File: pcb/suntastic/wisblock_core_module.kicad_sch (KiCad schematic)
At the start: 0 parts

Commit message: Add load switch and RAK connector
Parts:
- added J4: FBB04004-F40S1003K6M, FBB04004F40S1003K6M, symbol FBB04004-F40S1003K6M:FBB04004-F40S1003K6M
- added JP11: SolderJumper_2_Open, Jumper:SolderJumper-2_P1.3mm_Open_RoundedPad1.0x1.5mm, symbol Jumper:SolderJumper_2_Open
- added R2: 5.6M, symbol Device:R
- added R3: 9.3M, symbol Device:R
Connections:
- new net: JP11.2 (B), R2.1
- new net GND: J4.3, J4.39, J4.4, J4.40, J4.MP1, J4.MP2, J4.MP3, J4.MP4, R3.2
- new net V_boost_uvlo: JP11.1 (A)
- new net Vsupercap: R2.2, R3.1
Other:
- note added: "Voltage divider to measure the accumulator"

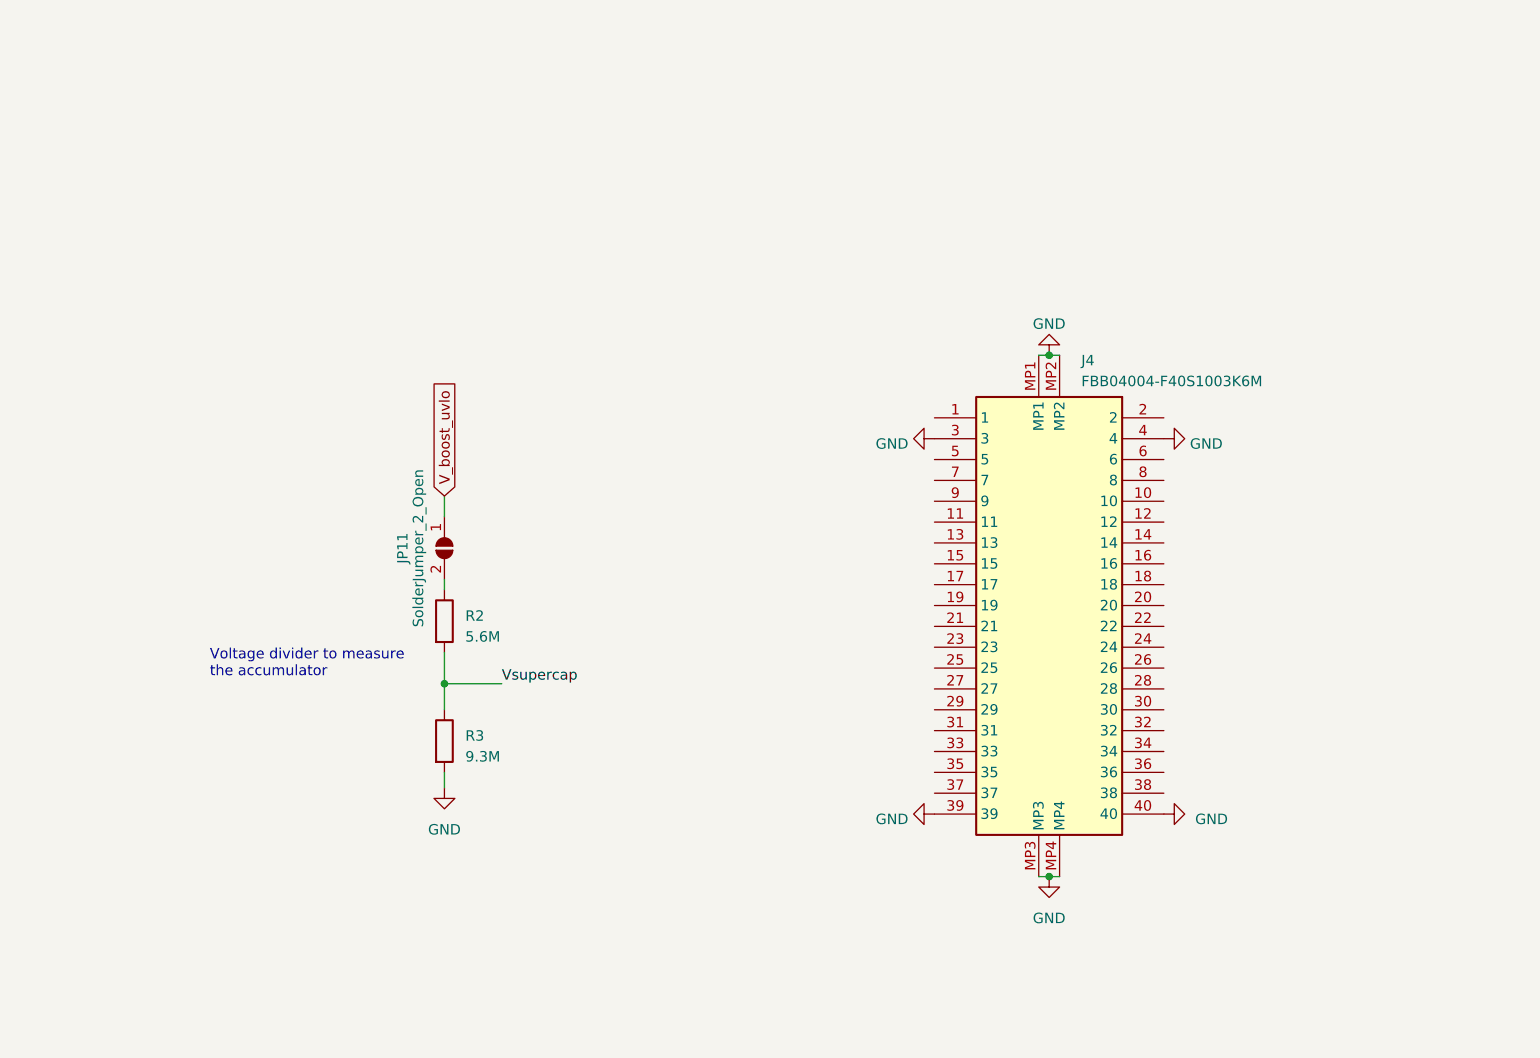
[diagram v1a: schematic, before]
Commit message: Add more doccstrings
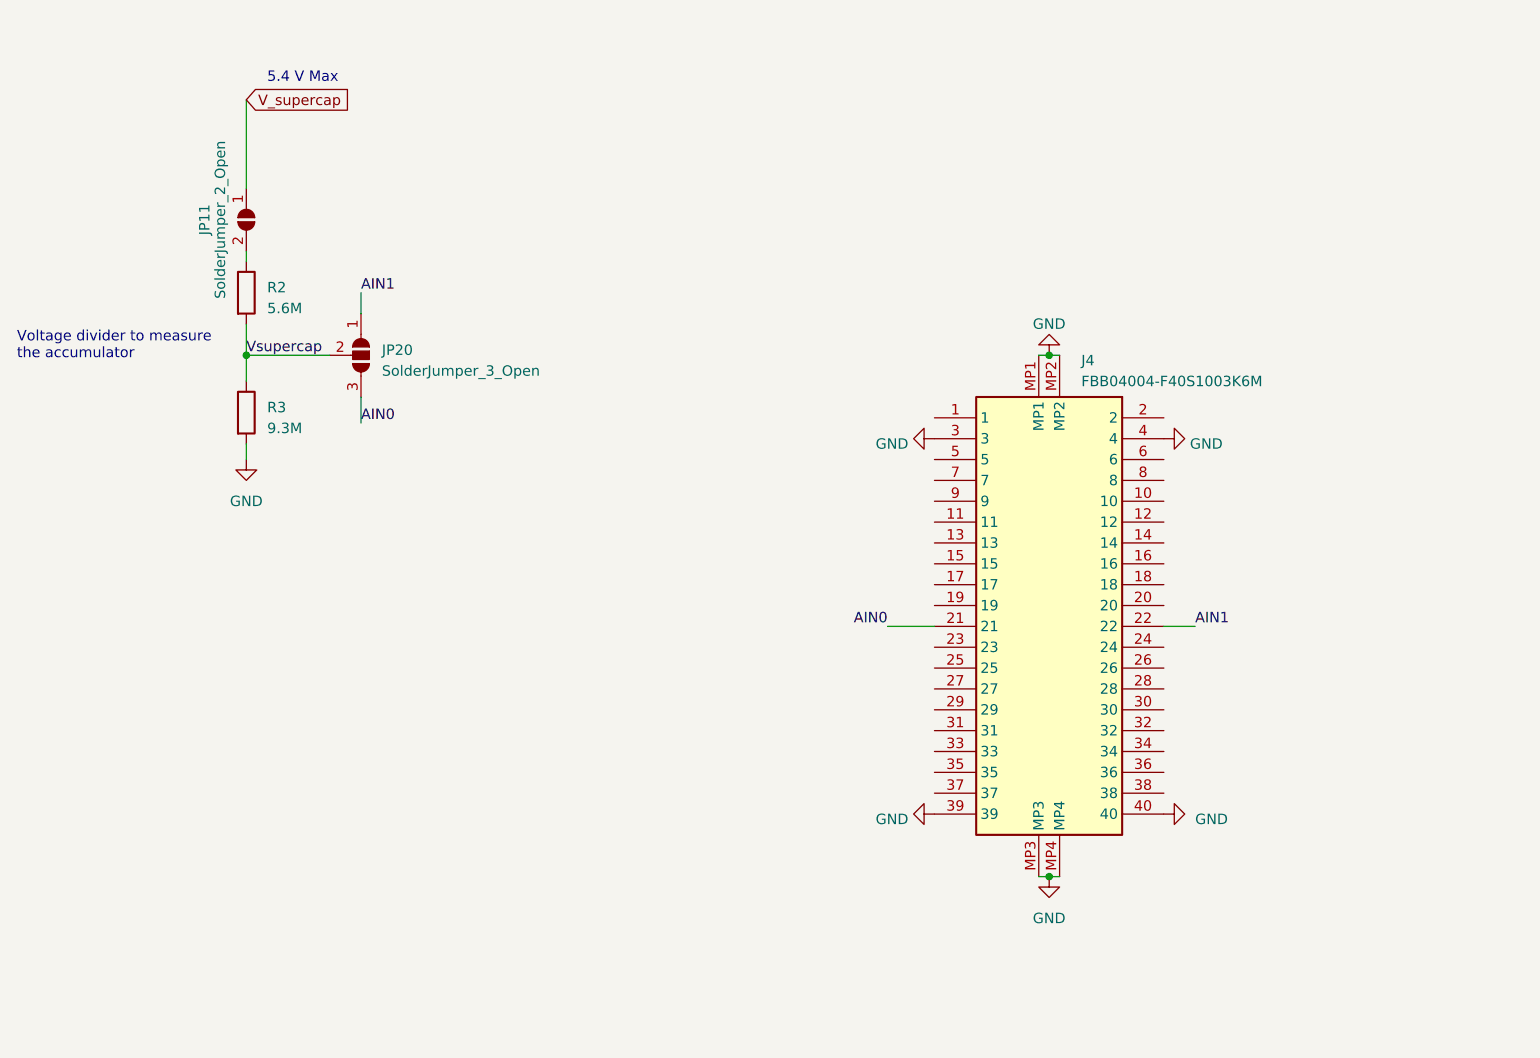
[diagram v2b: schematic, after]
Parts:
- added JP20: SolderJumper_3_Open, symbol Jumper:SolderJumper_3_Open
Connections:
- net Vsupercap: now also JP20.2 (C)
- net AIN0: now reaches J4.21
- net AIN0: now also JP20.3 (B)
- net AIN1: now reaches J4.22
- net AIN1: now also JP20.1 (A)
- net V_boost_uvlo renamed V_supercap
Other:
- note added: "5.4 V Max"
- moved on the sheet: JP11, R2, R3
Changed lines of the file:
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@@
   (junction (at 139.7 50.8) (diameter 0) (color 0 0 0 0)
   )
-  (junction (at 66.04 90.805) (diameter 0) (color 0 0 0 0)
+  (junction (at 41.91 50.8) (diameter 0) (color 0 0 0 0)
   )
   (junction (at 139.7 114.3) (diameter 0) (color 0 0 0 0)
   )
-  (wire (pts (xy 66.04 67.945) (xy 66.04 70.485))
-    (stroke (width 0) (type default))
-  )
-  (wire (pts (xy 66.04 101.6) (xy 66.04 103.505))
-    (stroke (width 0) (type default))
-  )
-  (wire (pts (xy 66.04 78.105) (xy 66.04 79.375))
+  (wire (pts (xy 41.91 19.685) (xy 41.91 30.48))
+    (stroke (width 0) (type default))
+  )
+  (wire (pts (xy 41.91 61.595) (xy 41.91 63.5))
+    (stroke (width 0) (type default))
+  )
+  (wire (pts (xy 55.88 55.88) (xy 55.88 59.055))
+    (stroke (width 0) (type default))
+  )
+  (wire (pts (xy 153.67 83.82) (xy 157.48 83.82))
+    (stroke (width 0) (type default))
+  )
+  (wire (pts (xy 120.015 83.82) (xy 125.73 83.82))
+    (stroke (width 0) (type default))
+  )
+  (wire (pts (xy 41.91 38.1) (xy 41.91 39.37))
     (stroke (width 0) (type default))
   )
@@
     (stroke (width 0) (type default))
   )
-  (wire (pts (xy 66.04 90.805) (xy 66.04 93.98))
+  (wire (pts (xy 41.91 50.8) (xy 41.91 53.975))
     (stroke (width 0) (type default))
   )
@@
     (stroke (width 0) (type default))
   )
+  (wire (pts (xy 55.88 43.18) (xy 55.88 45.72))
+    (stroke (width 0) (type default))
+  )
   (wire (pts (xy 139.7 114.3) (xy 140.97 114.3))
     (stroke (width 0) (type default))
@@
     (stroke (width 0) (type default))
   )
-  (wire (pts (xy 66.04 90.805) (xy 73.025 90.805))
-    (stroke (width 0) (type default))
-  )
-  (wire (pts (xy 66.04 86.995) (xy 66.04 90.805))
-    (stroke (width 0) (type default))
-  )
-  (text "Voltage divider to measure\nthe accumulator" (at 37.465 90.17 0)
-    (effects (font (size 1.27 1.27)) (justify left bottom))
-  )
-  (label "Vsupercap" (at 73.025 90.805 0) (fields_autoplaced)
-    (effects (font (size 1.27 1.27)) (justify left bottom))
-  )
-  (global_label "V_boost_uvlo" (shape input) (at 66.04 67.945 90) (fields_autoplaced)
+  (wire (pts (xy 41.91 50.8) (xy 52.07 50.8))
+    (stroke (width 0) (type default))
+  )
+  (wire (pts (xy 41.91 46.99) (xy 41.91 50.8))
+    (stroke (width 0) (type default))
+  )
+  (text "Voltage divider to measure\nthe accumulator" (at 13.97 51.435 0)
+    (effects (font (size 1.27 1.27)) (justify left bottom))
+  )
+  (text "5.4 V Max" (at 44.45 17.78 0)
+    (effects (font (size 1.27 1.27)) (justify left bottom))
+  )
+  (label "AIN0" (at 55.88 59.055 0) (fields_autoplaced)
+    (effects (font (size 1.27 1.27)) (justify left bottom))
+  )
+  (label "Vsupercap" (at 41.91 50.8 0) (fields_autoplaced)
+    (effects (font (size 1.27 1.27)) (justify left bottom))
+  )
+  (label "AIN1" (at 55.88 43.18 0) (fields_autoplaced)
+    (effects (font (size 1.27 1.27)) (justify left bottom))
+  )
+  (label "AIN1" (at 157.48 83.82 0) (fields_autoplaced)
+    (effects (font (size 1.27 1.27)) (justify left bottom))
+  )
+  (label "AIN0" (at 120.015 83.82 180) (fields_autoplaced)
+    (effects (font (size 1.27 1.27)) (justify right bottom))
+  )
+  (global_label "V_supercap" (shape input) (at 41.91 19.685 0) (fields_autoplaced)
     (effects (font (size 1.27 1.27)) (justify left))
-    (property "Intersheetrefs" "${INTERSHEET_REFS}" (at 66.04 52.8838 90)
+    (property "Intersheetrefs" "${INTERSHEET_REFS}" (at 55.4595 19.685 0)
       (effects (font (size 1.27 1.27)) (justify left) hide)
     )
   )
-  (symbol (lib_id "power:GND") (at 66.04 103.505 0) (unit 1)
-    (in_bom yes) (on_board yes) (dnp no) (fields_autoplaced)
-    (property "Reference" "#PWR010" (at 66.04 109.855 0)
-      (effects (font (size 1.27 1.27)) hide)
-    )
-    (property "Value" "GND" (at 66.04 108.585 0)
+  (symbol (lib_id "power:GND") (at 41.91 63.5 0) (unit 1)
+    (in_bom yes) (on_board yes) (dnp no) (fields_autoplaced)
+    (property "Reference" "#PWR010" (at 41.91 69.85 0)
+      (effects (font (size 1.27 1.27)) hide)
+    )
+    (property "Value" "GND" (at 41.91 68.58 0)
       (effects (font (size 1.27 1.27)))
     )
-    (property "Footprint" "" (at 66.04 103.505 0)
-      (effects (font (size 1.27 1.27)) hide)
-    )
-    (property "Datasheet" "" (at 66.04 103.505 0)
+    (property "Footprint" "" (at 41.91 63.5 0)
+      (effects (font (size 1.27 1.27)) hide)
+    )
+    (property "Datasheet" "" (at 41.91 63.5 0)
       (effects (font (size 1.27 1.27)) hide)
     )
@@
     )
   )
-  (symbol (lib_id "Device:R") (at 66.04 97.79 0) (unit 1)
-    (in_bom yes) (on_board yes) (dnp no) (fields_autoplaced)
-    (property "Reference" "R3" (at 68.58 97.155 0)
-      (effects (font (size 1.27 1.27)) (justify left))
-    )
-    (property "Value" "9.3M" (at 68.58 99.695 0)
-      (effects (font (size 1.27 1.27)) (justify left))
-    )
-    (property "Footprint" "" (at 64.262 97.79 90)
-      (effects (font (size 1.27 1.27)) hide)
-    )
-    (property "Datasheet" "~" (at 66.04 97.79 0)
+  (symbol (lib_id "Device:R") (at 41.91 57.785 0) (unit 1)
+    (in_bom yes) (on_board yes) (dnp no) (fields_autoplaced)
+    (property "Reference" "R3" (at 44.45 57.15 0)
+      (effects (font (size 1.27 1.27)) (justify left))
+    )
+    (property "Value" "9.3M" (at 44.45 59.69 0)
+      (effects (font (size 1.27 1.27)) (justify left))
+    )
+    (property "Footprint" "" (at 40.132 57.785 90)
+      (effects (font (size 1.27 1.27)) hide)
+    )
+    (property "Datasheet" "~" (at 41.91 57.785 0)
       (effects (font (size 1.27 1.27)) hide)
     )
@@
     )
   )
-  (symbol (lib_id "Device:R") (at 66.04 83.185 0) (unit 1)
-    (in_bom yes) (on_board yes) (dnp no) (fields_autoplaced)
-    (property "Reference" "R2" (at 68.58 82.55 0)
-      (effects (font (size 1.27 1.27)) (justify left))
-    )
-    (property "Value" "5.6M" (at 68.58 85.09 0)
-      (effects (font (size 1.27 1.27)) (justify left))
-    )
-    (property "Footprint" "" (at 64.262 83.185 90)
-      (effects (font (size 1.27 1.27)) hide)
-    )
-    (property "Datasheet" "~" (at 66.04 83.185 0)
+  (symbol (lib_id "Device:R") (at 41.91 43.18 0) (unit 1)
+    (in_bom yes) (on_board yes) (dnp no) (fields_autoplaced)
+    (property "Reference" "R2" (at 44.45 42.545 0)
+      (effects (font (size 1.27 1.27)) (justify left))
+    )
+    (property "Value" "5.6M" (at 44.45 45.085 0)
+      (effects (font (size 1.27 1.27)) (justify left))
+    )
+    (property "Footprint" "" (at 40.132 43.18 90)
+      (effects (font (size 1.27 1.27)) hide)
+    )
+    (property "Datasheet" "~" (at 41.91 43.18 0)
       (effects (font (size 1.27 1.27)) hide)
     )
@@
     )
   )
-  (symbol (lib_id "Jumper:SolderJumper_2_Open") (at 66.04 74.295 270) (unit 1)
+  (symbol (lib_id "Jumper:SolderJumper_2_Open") (at 41.91 34.29 270) (unit 1)
     (in_bom yes) (on_board yes) (dnp no)
-    (property "Reference" "JP11" (at 60.96 74.295 0)
+    (property "Reference" "JP11" (at 36.83 34.29 0)
       (effects (font (size 1.27 1.27)))
     )
-    (property "Value" "SolderJumper_2_Open" (at 62.865 74.295 0)
+    (property "Value" "SolderJumper_2_Open" (at 38.735 34.29 0)
       (effects (font (size 1.27 1.27)))
     )
-    (property "Footprint" "Jumper:SolderJumper-2_P1.3mm_Open_RoundedPad1.0x1.5mm" (at 66.04 74.295 0)
-      (effects (font (size 1.27 1.27)) hide)
-    )
-    (property "Datasheet" "~" (at 66.04 74.295 0)
+    (property "Footprint" "Jumper:SolderJumper-2_P1.3mm_Open_RoundedPad1.0x1.5mm" (at 41.91 34.29 0)
+      (effects (font (size 1.27 1.27)) hide)
+    )
+    (property "Datasheet" "~" (at 41.91 34.29 0)
       (effects (font (size 1.27 1.27)) hide)
     )
@@
         )
       )
+    )
+  )
+  (symbol (lib_id "Jumper:SolderJumper_3_Open") (at 55.88 50.8 270) (unit 1)
+    (in_bom yes) (on_board yes) (dnp no) (fields_autoplaced)
+    (property "Reference" "JP20" (at 58.42 50.165 90)
+      (effects (font (size 1.27 1.27)) (justify left))
+    )
+    (property "Value" "SolderJumper_3_Open" (at 58.42 52.705 90)
+      (effects (font (size 1.27 1.27)) (justify left))
+    )
+    (property "Footprint" "" (at 55.88 50.8 0)
+      (effects (font (size 1.27 1.27)) hide)
+    )
+    (property "Datasheet" "~" (at 55.88 50.8 0)
+      (effects (font (size 1.27 1.27)) hide)
+    )
+    (pin "1")
+    (pin "2")
+    (pin "3")
+    (instances
+      (project "suntastic"
+        (path "/4d5a6178-89d6-4824-ac30-5dee40aabff2/6649cb35-9eb9-427a-adc1-370521538cf9"
+          (reference "JP20") (unit 1)
+        )
+      )

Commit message: add wdt
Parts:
- added C17, C18: 0.1uF, symbol Device:C
- added FB1, FB2, FB3: FerriteBead, symbol Device:FerriteBead
- added J7, J8: Conn_01x04_Pin, symbol Connector:Conn_01x04_Pin
- added J9: Conn_01x08_Pin, symbol Connector:Conn_01x08_Pin
- added TP10: IO1, symbol Connector:TestPoint
- added TP11: IO6, symbol Connector:TestPoint
- added TP12: IO8, symbol Connector:TestPoint
- added TP13: IO7, symbol Connector:TestPoint
- added TP4: LED2, symbol Connector:TestPoint
- added TP5: LED1, symbol Connector:TestPoint
- added TP6: IO4, symbol Connector:TestPoint
- added TP7: IO2, symbol Connector:TestPoint
- added TP8: IO5, symbol Connector:TestPoint
- added TP9: IO3, symbol Connector:TestPoint
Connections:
- net AIN0: now also C18.1
- net GND: now also C17.2, C18.2, J7.2 (Pin_2), J8.2 (Pin_2)
- net at J4.1: now also J4.2, FB1.2
- net TXD0: now reaches J4.11
- net TXD0: now also J8.3 (Pin_3)
- net RXD0: now reaches J4.12
- net RXD0: now also J8.4 (Pin_4)
- net nrf_reset: now reaches J4.13
- net nrf_reset: now also C17.1
- net at J4.14: now also TP5.1
- net at J4.15: now also TP4.1
- net IO8: now reaches J4.16
- net IO8: now also J9.8 (Pin_8), TP12.1
- net BOOT0: now reaches J4.23
- net BOOT0: now also J7.1 (Pin_1)
- net IO7: now reaches J4.24
- net IO7: now also J9.7 (Pin_7), TP13.1
- net IO1: now reaches J4.29
- net IO1: now also J9.1 (Pin_1), TP10.1
- net IO2: now reaches J4.30
- net IO2: now also J9.2 (Pin_2), TP7.1
- net IO3: now reaches J4.31
- net IO3: now also J9.3 (Pin_3), TP9.1
- net IO4: now reaches J4.32
- net IO4: now also J9.4 (Pin_4), TP6.1
- net TXD1: now reaches J4.33
- net TXD1: now also J7.3 (Pin_3)
- net RXD1: now reaches J4.34
- net RXD1: now also J7.4 (Pin_4)
- net IO5: now reaches J4.37
- net IO5: now also J9.5 (Pin_5), TP8.1
- net IO6: now reaches J4.38
- net IO6: now also J9.6 (Pin_6), TP11.1
- net at J4.5: now also FB2.2
- net at J4.6: now also FB3.1
- new net 3.3V: FB2.1, FB3.2
- new net V_boost_uvlo: FB1.1
- no-connect marks 0 -> 14
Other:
- note added: "5.2 V Max"
- note removed: "5.4 V Max"
